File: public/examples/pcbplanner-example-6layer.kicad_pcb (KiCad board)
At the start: 6 copper layers, 80 x 60 mm, 0 parts

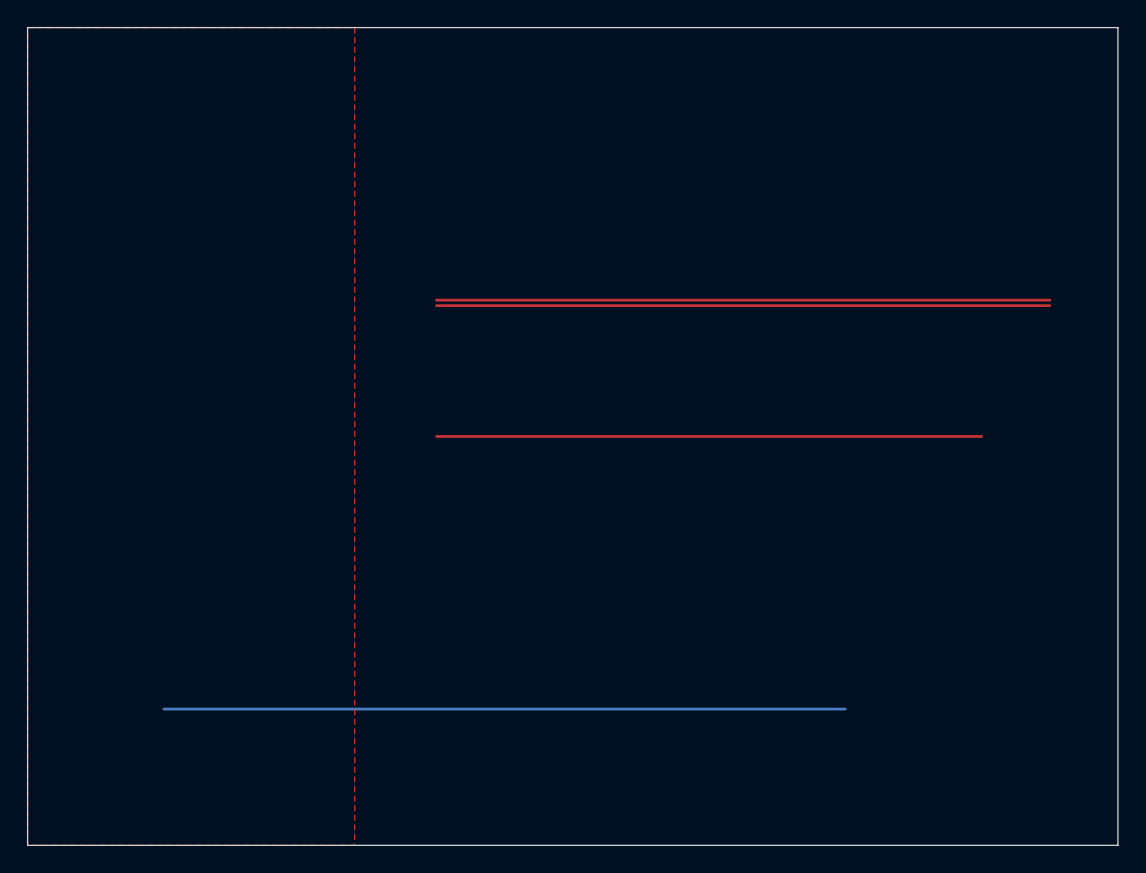
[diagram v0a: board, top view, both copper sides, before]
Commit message: KiCad: check the routed pairs and nets of a project
Load a project folder, several files (.kicad_pcb + .kicad_pro) or one board. The new
Routing Check measures every differential pair (KiCad's MatchDpSuffix rule) and every
checked net per layer: width, gap and coupled length from the track geometry, the
impedance from the field solver (same solve as the width table), skew in mm and ps,
length, vias and loss at the interface's Nyquist frequency, with pass / warning / fail
against the interface limits in interfaces.ts or a plain target. Net classes are read
from the .kicad_pro for KiCad 6 to 10 (each schema version). Targets are suggested from
names and editable; only overrides go into the URL. The example board now includes a
pair that goes wrong at a layer change and one with a skew problem.

Co-Authored-By: Claude Opus 5.5 <noreply@anthropic.com>
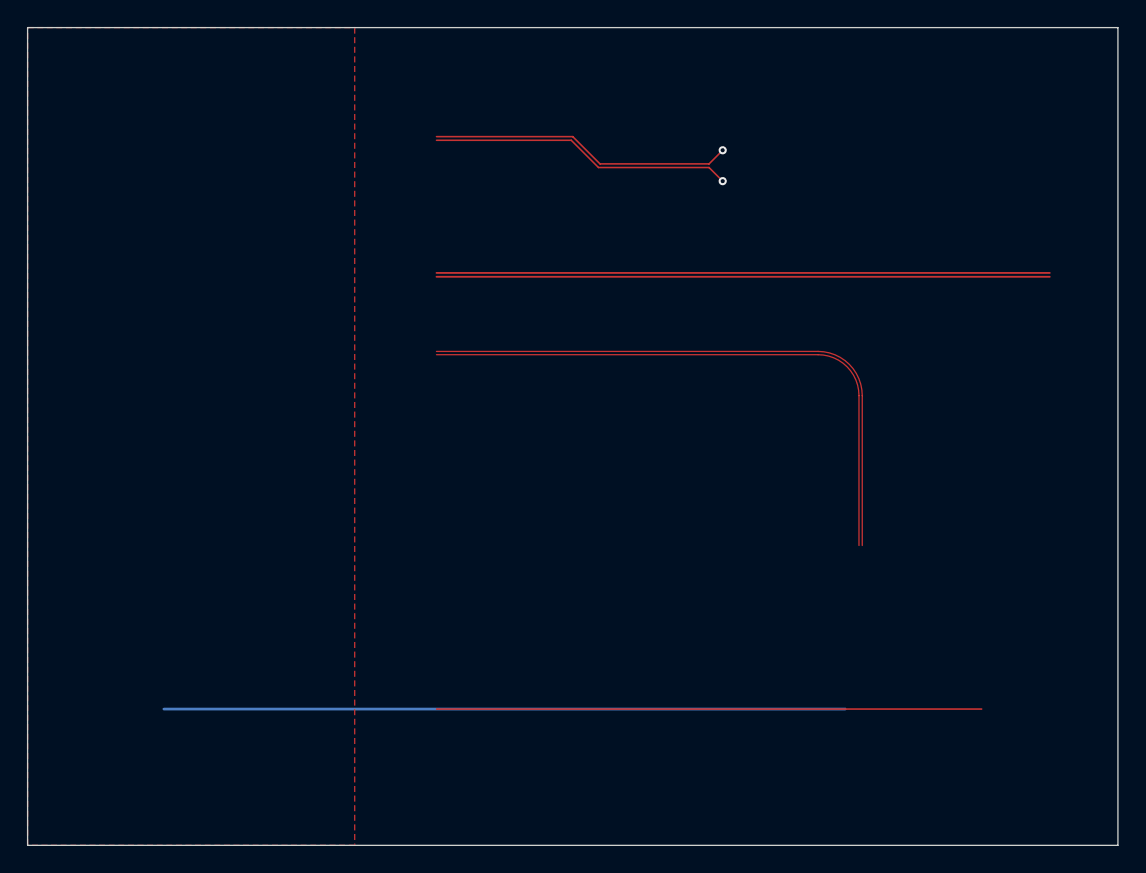
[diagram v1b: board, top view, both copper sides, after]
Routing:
- net /USB_D-: track 0.00 -> 46.6 mm, vias 0 -> 1
- net /USB_D+: track 0.00 -> 46.6 mm, vias 0 -> 1
- net /HDMI_D0-: track 0.00 -> 44.0 mm
- net /HDMI_D0+: track 0.00 -> 43.6 mm
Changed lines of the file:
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@@
 	(net 5 "/CLK")
 	(net 6 "/SDA")
+	(net 7 "/USB_D+")
+	(net 8 "/USB_D-")
+	(net 9 "/HDMI_D0+")
+	(net 10 "/HDMI_D0-")
 	(gr_rect
 		(start 100 100)
@@
 	)
 	(segment
-		(start 130 120)
-		(end 175 120)
-		(width 0.2)
+		(start 130 108)
+		(end 140 108)
+		(width 0.117)
+		(layer "F.Cu")
+		(net 7)
+	)
+	(segment
+		(start 140 108)
+		(end 142 110)
+		(width 0.117)
+		(layer "F.Cu")
+		(net 7)
+	)
+	(segment
+		(start 142 110)
+		(end 150 110)
+		(width 0.117)
+		(layer "F.Cu")
+		(net 7)
+	)
+	(segment
+		(start 150 110)
+		(end 151 109)
+		(width 0.117)
+		(layer "F.Cu")
+		(net 7)
+	)
+	(segment
+		(start 130 108.267)
+		(end 139.8894 108.267)
+		(width 0.117)
+		(layer "F.Cu")
+		(net 8)
+	)
+	(segment
+		(start 139.8894 108.267)
+		(end 141.8894 110.267)
+		(width 0.117)
+		(layer "F.Cu")
+		(net 8)
+	)
+	(segment
+		(start 141.8894 110.267)
+		(end 150 110.267)
+		(width 0.117)
+		(layer "F.Cu")
+		(net 8)
+	)
+	(segment
+		(start 150 110.267)
+		(end 151 111.267)
+		(width 0.117)
+		(layer "F.Cu")
+		(net 8)
+	)
+	(via
+		(at 151 109)
+		(size 0.6)
+		(drill 0.3)
+		(layers "F.Cu" "B.Cu")
+		(net 7)
+	)
+	(via
+		(at 151 111.267)
+		(size 0.6)
+		(drill 0.3)
+		(layers "F.Cu" "B.Cu")
+		(net 8)
+	)
+	(segment
+		(start 151 109)
+		(end 151.958 109.958)
+		(width 0.2)
+		(layer "In2.Cu")
+		(net 7)
+	)
+	(segment
+		(start 151.958 109.958)
+		(end 175 109.958)
+		(width 0.2)
+		(layer "In2.Cu")
+		(net 7)
+	)
+	(segment
+		(start 151 111.267)
+		(end 151.959 110.308)
+		(width 0.2)
+		(layer "In2.Cu")
+		(net 8)
+	)
+	(segment
+		(start 151.959 110.308)
+		(end 175 110.308)
+		(width 0.2)
+		(layer "In2.Cu")
+		(net 8)
+	)
+	(segment
+		(start 130 118)
+		(end 175 118)
+		(width 0.133)
 		(layer "F.Cu")
 		(net 3)
 	)
 	(segment
-		(start 130 120.4)
-		(end 175 120.4)
-		(width 0.2)
+		(start 130 118.283)
+		(end 175 118.283)
+		(width 0.133)
 		(layer "F.Cu")
 		(net 4)
 	)
 	(segment
-		(start 130 130)
-		(end 170 130)
-		(width 0.2)
+		(start 130 124)
+		(end 158 124)
+		(width 0.09)
+		(layer "F.Cu")
+		(net 9)
+	)
+	(arc
+		(start 158 124)
+		(mid 160.1213 124.8787)
+		(end 161 127)
+		(width 0.09)
+		(layer "F.Cu")
+		(net 9)
+	)
+	(segment
+		(start 161 127)
+		(end 161 138)
+		(width 0.09)
+		(layer "F.Cu")
+		(net 9)
+	)
+	(segment
+		(start 130 123.76)
+		(end 158 123.76)
+		(width 0.09)
+		(layer "F.Cu")
+		(net 10)
+	)
+	(arc
+		(start 158 123.76)
+		(mid 160.291 124.709)
+		(end 161.24 127)
+		(width 0.09)
+		(layer "F.Cu")
+		(net 10)
+	)
+	(segment
+		(start 161.24 127)
+		(end 161.24 138)
+		(width 0.09)
+		(layer "F.Cu")
+		(net 10)
+	)
+	(segment
+		(start 130 150)
+		(end 170 150)
+		(width 0.12)
 		(layer "F.Cu")
 		(net 5)
@@
 		(start 110 145)
 		(end 170 145)
-		(width 0.2)
+		(width 0.121)
 		(layer "In2.Cu")
 		(net 5)

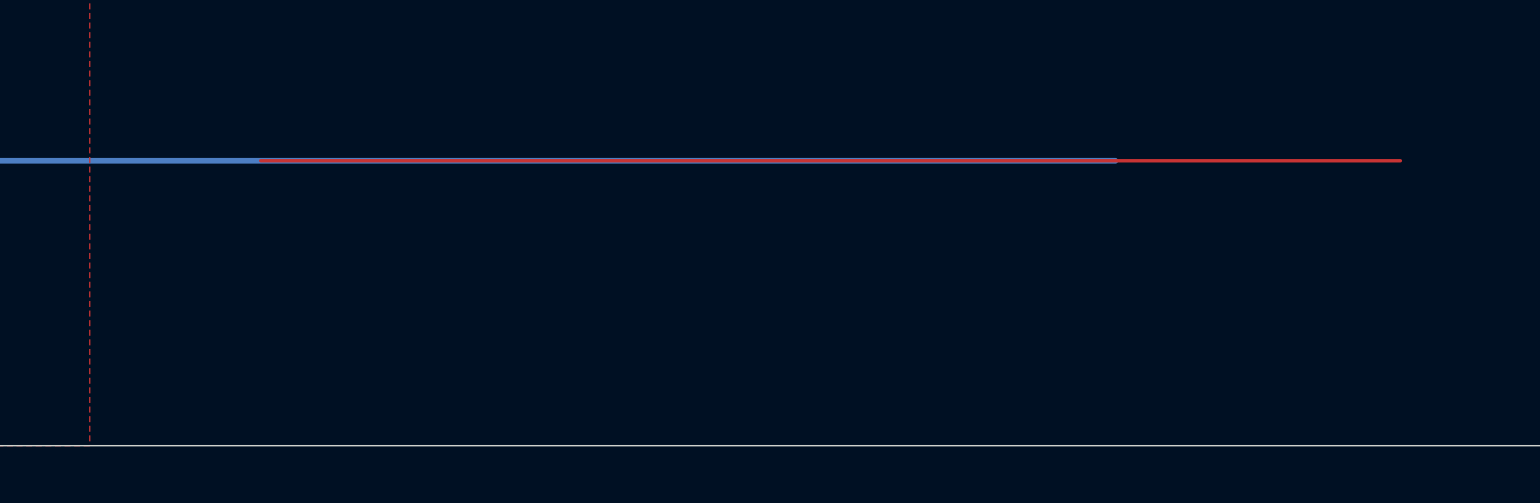
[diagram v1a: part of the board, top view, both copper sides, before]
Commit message: Thermal tab: Solve button; example board gets parts; e2e false alarms fixed
- Thermal: a Solve button runs the solve; the last map stays and is marked
  out of date when the inputs change. A board without footprints says it
  has no parts to heat instead of only disabling Add part.
- Thermal and Power warn when a board's zones are not filled in the file
  (planes are then left out of the result).
- Example board: a power section (J1 +5V connector, U1 SOT-223 3.3 V
  regulator, U2 QFN with exposed pad and thermal vias, C1) with +5V, +3V3
  and GND tracks, so Power, Thermal and Clearance work on the example.
- E-series neighbours: a value within a part per billion of a series value
  is that value (100 nF typed in is 1.0000000000000001e-7 F), so the RC
  filter no longer lists an extra standard pair.
- e2e: long dropdowns are sampled, a busy message must end in an ellipsis
  (a cited title "Solving the Metric Pitch BGA..." is not one), and a
  restore that leaves every result the same is not a failure.

Co-Authored-By: Claude Opus 5.5 <noreply@anthropic.com>
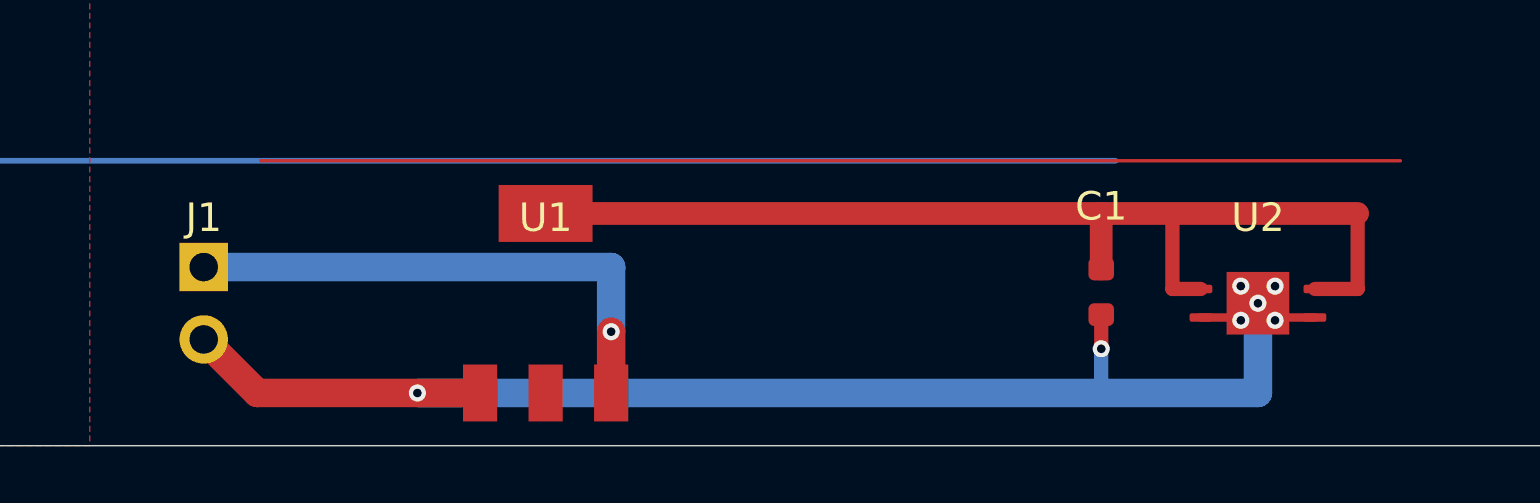
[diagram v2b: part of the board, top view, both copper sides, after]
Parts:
- added C1: 10uF, Capacitor_SMD:C_0603_1608Metric, F.Cu at (159.5, 154.6)
- added J1: +5V in, Connector_PinHeader_2.54mm:PinHeader_1x02_P2.54mm_Vertical, F.Cu at (128.0, 155.0)
- added U1: AMS1117-3.3, Package_TO_SOT_SMD:SOT-223-3_TabPin2, F.Cu at (140.0, 155.0)
- added U2: MCU, Package_DFN_QFN:QFN-16-1EP_4x4mm_P0.65mm, F.Cu at (165.0, 155.0)
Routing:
- net GND: track 0.00 -> 47.7 mm, vias 0 -> 7
- net +3V3: track 0.00 -> 36.6 mm
- net +5V: track 0.00 -> 18.7 mm, vias 0 -> 1
